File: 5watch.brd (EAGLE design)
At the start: 74 x 52 mm, 33 parts, among them U1 ATMEGA328P_TQFP, Y2 32.768 kHz

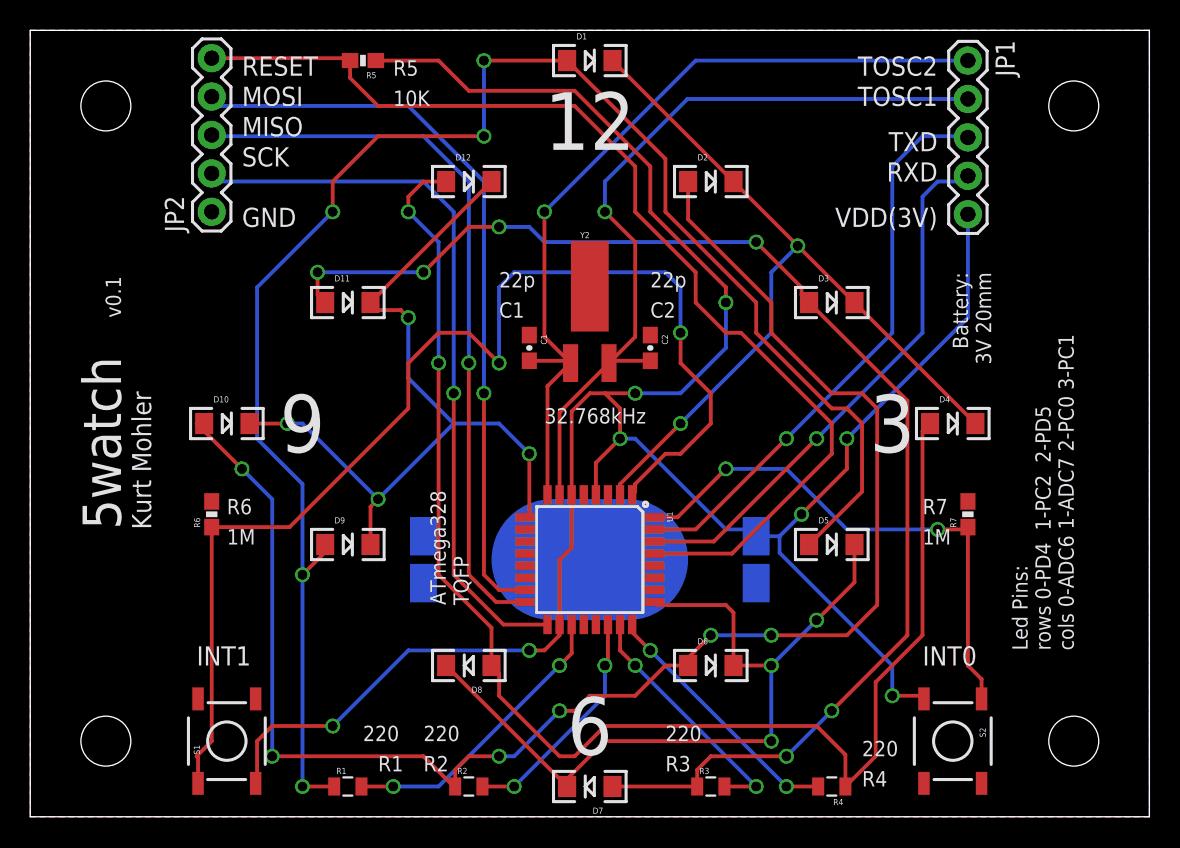
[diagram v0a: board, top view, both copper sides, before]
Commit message: fixed led connections, wired ADC6 and ADC7 to ground, removed TOSC pins from breakout, shrunk board, reversed button pin voltages
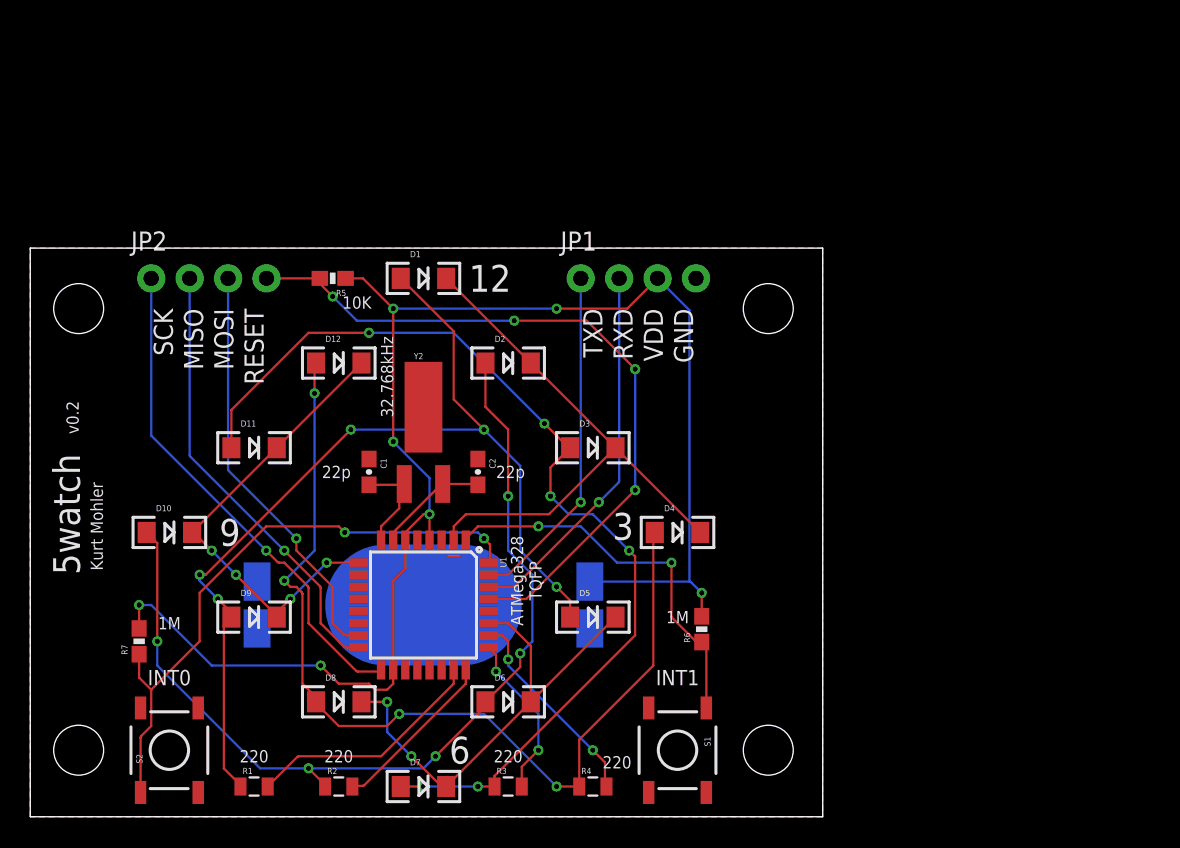
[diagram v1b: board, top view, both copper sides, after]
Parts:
- JP1, JP2: device SparkFun-Connectors:1X05 -> SparkFun-Connectors:1X04_NO_SILK_ALL_ROUND
- moved STANDOFF4 67.2 mm to (3.20, 33.6)
- moved STANDOFF1 61.1 mm to (48.8, 4.40)
- moved R7 55.4 mm to (7.20, 11.6)
- moved S2 51.8 mm to (9.20, 4.40), turned to 90 degrees
- moved STANDOFF2 35.0 mm to (48.8, 33.6)
- moved R6 33.3 mm to (44.4, 12.4)
- moved S1 29.8 mm to (42.8, 4.40), turned to 270 degrees
- moved JP1 29.4 mm to (36.4, 35.6), turned to 0 degrees
- moved D4 19.6 mm to (42.8, 18.8)
- moved D3 18.5 mm to (37.2, 24.4)
- moved D1 18.1 mm to (26.0, 35.6)
- moved D2 18.0 mm to (31.6, 30.0)
- moved D5 16.5 mm to (37.2, 13.2)
- moved R4 15.8 mm to (37.2, 2.00), turned to 0 degrees
- moved D12 14.8 mm to (20.4, 30.0)
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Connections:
- removed net TOSC1: C2.2, JP1.2, U1.7, Y2.X2
- removed net TOSC2: C1.2, JP1.1, U1.8, Y2.X1
- new net N$10: C1.2, U1.8, Y2.X1
- new net N$8: C2.2, U1.7, Y2.X2
- net GND: now also JP1.4, S1.3, S2.3, U1.19, U1.22; no longer JP2.1, R6.2, R7.2
- net MISO: now also JP2.2; no longer JP2.3
- net MOSI: now also JP2.3; no longer JP2.4
- net N$13: now also U1.26; no longer U1.24
- net N$19: now also U1.25; no longer U1.23
- net N$20: now also U1.24; no longer U1.22
- net N$21: now also U1.23; no longer U1.19
- net N$6: now also U1.27; no longer U1.25
- net RESET: now also JP2.4; no longer JP2.5
- net RXD: now also JP1.2; no longer JP1.4
- net SCK: now also JP2.1; no longer JP2.2
- net TXD: now also JP1.1; no longer JP1.3
- net VDD: now also JP1.3, R6.2, R7.2; no longer JP1.5, S1.3, S2.3
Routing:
- net TOSC2: track 55.0 -> 0.00 mm, vias 1 -> 0
- net TOSC1: track 53.8 -> 0.00 mm, vias 1 -> 0
- net N$9: track 79.4 -> 25.8 mm
- net VDD: track 151.2 -> 102.0 mm, vias 8 -> 7
- net N$4: track 111.9 -> 65.3 mm
- net N$1: track 105.7 -> 62.7 mm, vias 6 -> 5
- net N$3: track 93.1 -> 63.7 mm, vias 2 -> 4
- net RESET: track 71.1 -> 47.8 mm, vias 0 -> 4
- net N$7: track 53.5 -> 30.8 mm
- net MOSI: track 49.4 -> 27.7 mm
- net N$2: track 87.8 -> 66.4 mm
- net N$6: track 53.1 -> 32.0 mm, vias 3 -> 2
- net MISO: track 48.7 -> 29.5 mm
- net N$5: track 55.3 -> 37.5 mm, vias 2 -> 0
- net SCK: track 48.6 -> 33.5 mm
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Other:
- board size 74 x 52 mm -> 52.4 x 37.6 mm
- board text added: "ATMega328 TQFP"
- board text added: "Coin cell 3V 20mm"
- board text added: "VDD"
- board text added: "v0.2"
- board text removed: "ATmega328 TQFP"
- board text removed: "Battery: 3V 20mm"
- board text removed: "C1"
- board text removed: "C2"
- board text removed: "Led Pins: rows 0-PD4 1-PC2 2-PD5 cols 0-ADC6 1-ADC7 2-PC0 3-PC1"
- board text removed: "R1"
- board text removed: "R2"
- board text removed: "R3"
- board text removed: "R4"
- board text removed: "R5"
- board text removed: "R6"
- board text removed: "R7"
- board text removed: "TOSC1"
- board text removed: "TOSC2"
- board text removed: "VDD(3V)"
- board text removed: "v0.1"

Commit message: moved traces around to increase ground fill connectivity
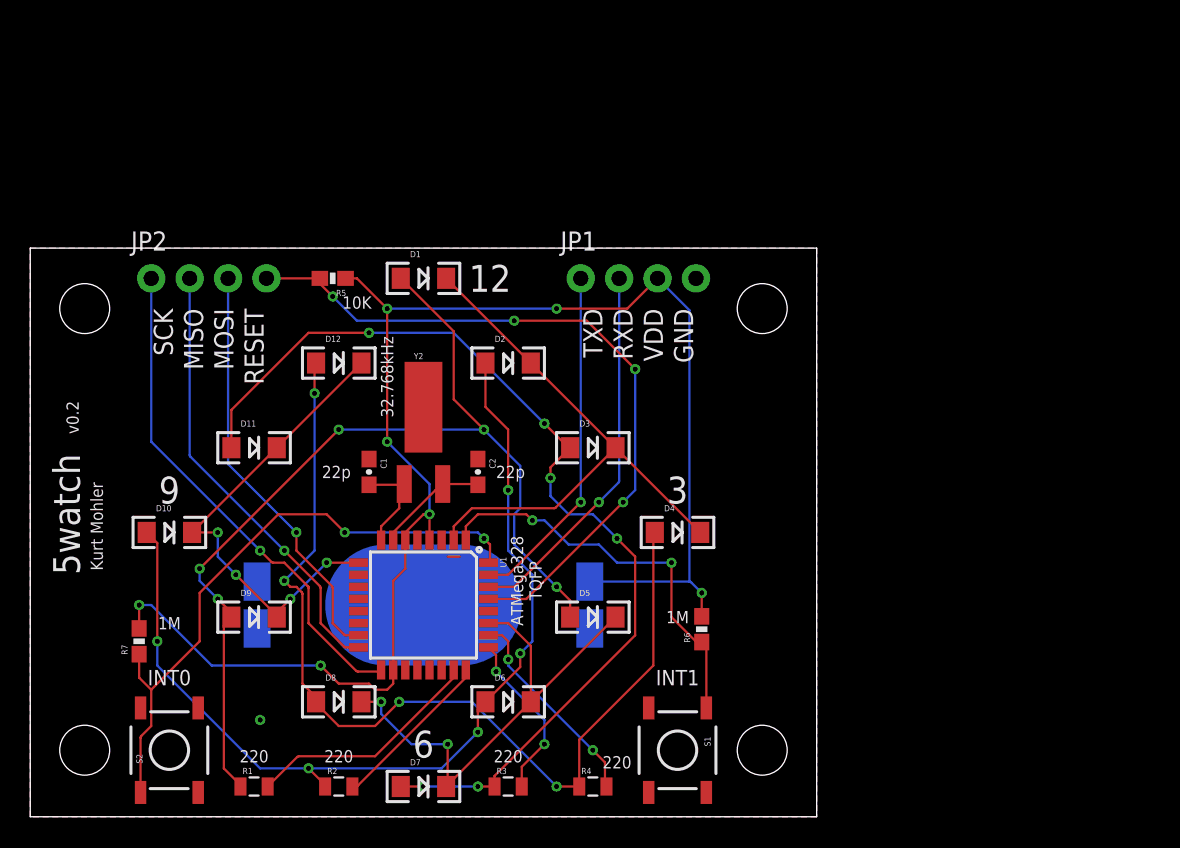
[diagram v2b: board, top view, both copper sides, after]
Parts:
- moved STANDOFF3 0.40 mm to (3.60, 4.40)
- moved STANDOFF4 0.40 mm to (3.60, 33.6)
- moved STANDOFF1 0.40 mm to (48.4, 4.40)
- moved STANDOFF2 0.40 mm to (48.4, 33.6)
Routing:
- net N$6: track 32.0 -> 33.5 mm
- net N$9: track 25.8 -> 27.0 mm
- net N$1: track 62.7 -> 63.8 mm
- net N$7: track 30.8 -> 31.7 mm
- net N$3: track 63.7 -> 64.4 mm
- net N$23: track 40.2 -> 40.9 mm
- net N$4: track 65.3 -> 65.9 mm
- net GND: track 0.91 -> 0.80 mm, vias 0 -> 1
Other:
- board size 52.4 x 37.6 mm -> 52 x 37.6 mm
